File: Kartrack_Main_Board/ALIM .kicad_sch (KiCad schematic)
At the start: 22 parts, among them IC1 MIC3172YM, J4 Conn_01x02_Socket, J5 Conn_01x02_Socket, U4 BQ21040DBV, U5 BU33SD5WG

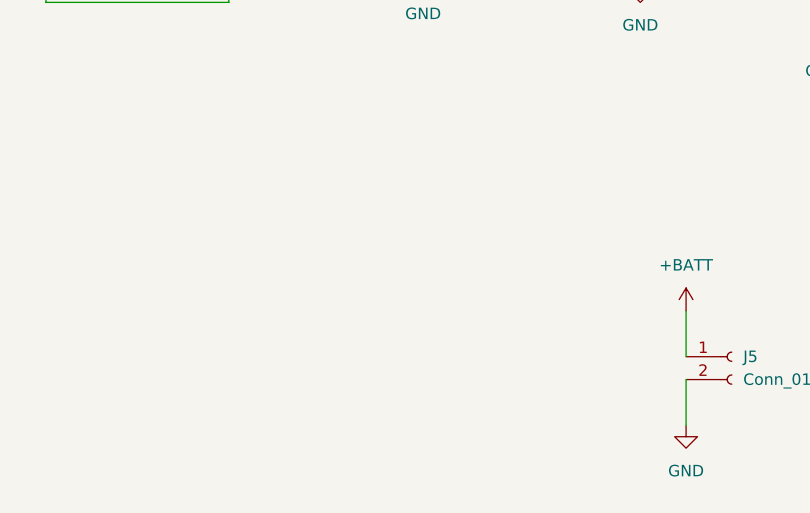
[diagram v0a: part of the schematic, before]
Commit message: add adc batt
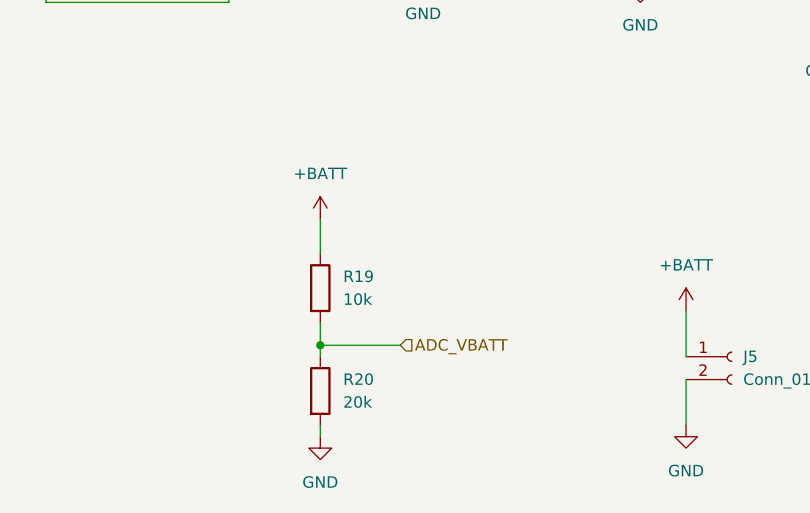
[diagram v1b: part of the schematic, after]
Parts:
- added R19: 10k, symbol Device:R
- added R20: 20k, symbol Device:R
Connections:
- net +BATT: now also R19.1
- net GND: now also R20.2
- new net ADC_VBATT: R19.2, R20.1

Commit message: adc
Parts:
- R19, R20: footprint (none) -> Resistor_SMD:R_0603_1608Metric
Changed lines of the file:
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@@
 			)
 		)
-		(property "Footprint" ""
+		(property "Footprint" "Resistor_SMD:R_0603_1608Metric"
 			(at 164.592 121.92 90)
 			(effects
@@
 			)
 		)
-		(property "Footprint" ""
+		(property "Footprint" "Resistor_SMD:R_0603_1608Metric"
 			(at 164.592 133.35 90)
 			(effects
